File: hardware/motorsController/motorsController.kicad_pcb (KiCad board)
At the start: 2 copper layers, 12 parts, among them J1 batery_connector, M1 Motor_DC, U1 VNH5019A-E

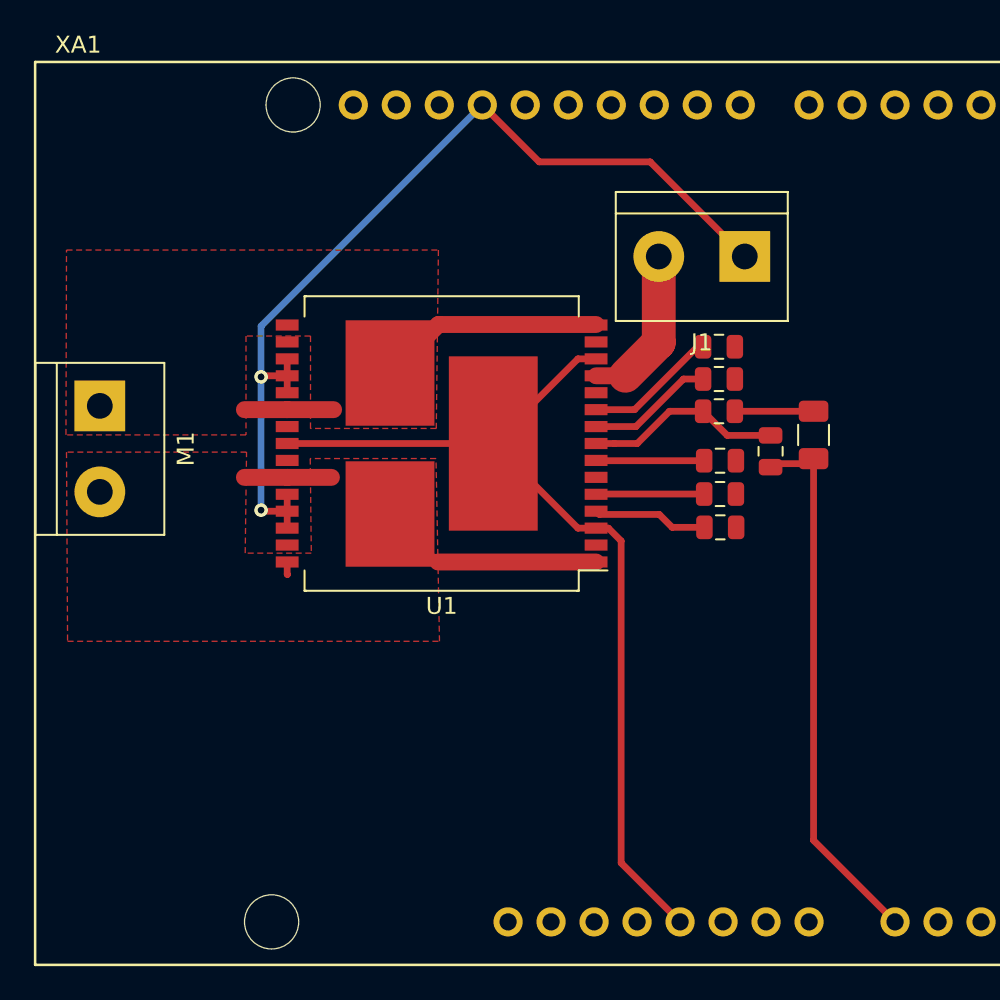
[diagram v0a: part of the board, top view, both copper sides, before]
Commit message: reposition motor terminals on both sides of the dirver
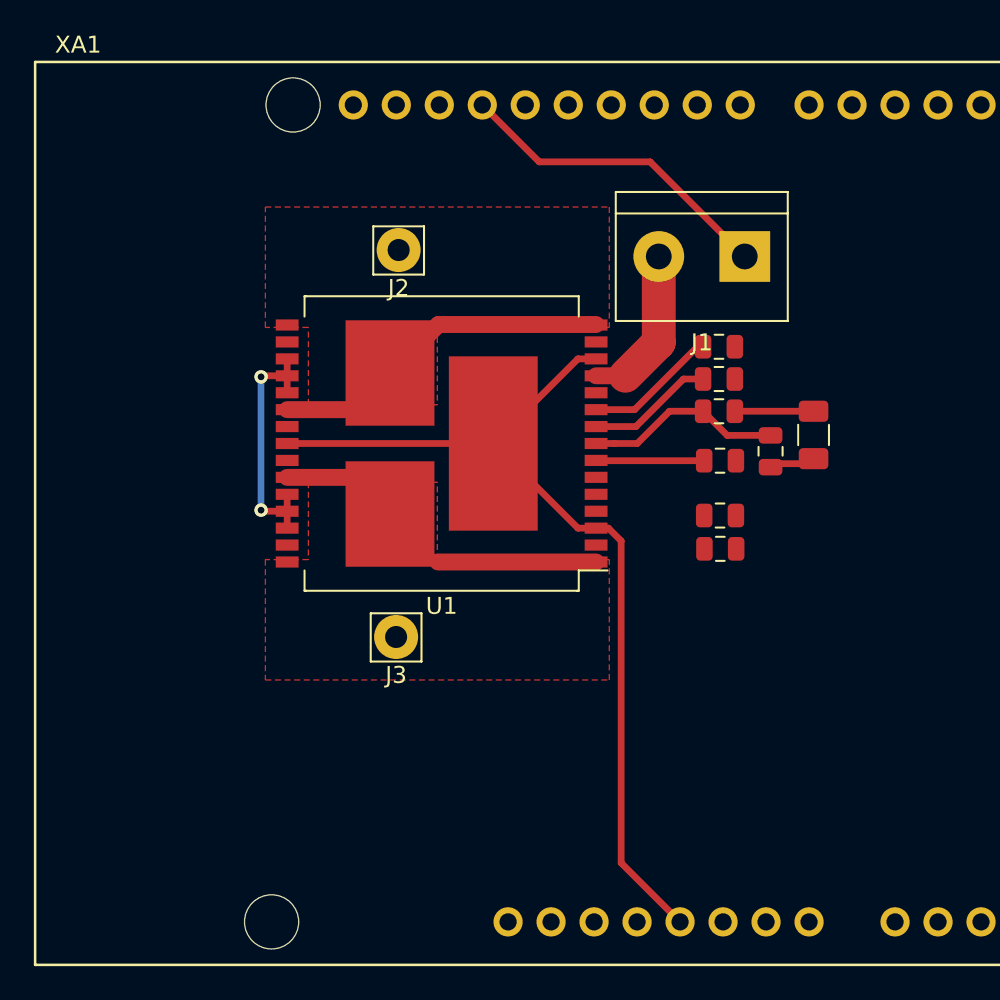
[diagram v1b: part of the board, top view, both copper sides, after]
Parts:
- removed M1: Motor_DC, TerminalBlock:TerminalBlock_bornier-2_P5.08mm
- added J2: Screw_Terminal_01x01, Connector_Pin:Pin_D1.3mm_L11.3mm_W2.8mm_Flat, F.Cu at (47.0, 38.1)
- added J3: Screw_Terminal_01x01, Connector_Pin:Pin_D1.3mm_L11.3mm_W2.8mm_Flat, F.Cu at (46.8, 61.0)
- moved R3 1.27 mm to (66.0, 55.8)
- moved R6 1.27 mm to (66.0, 53.8)
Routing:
- net /motor_right_front_cs: track 32.0 -> 2.66 mm
- net GND: track 60.4 -> 38.9 mm
- net Net-(R3-Pad1): track 6.79 -> 0.00 mm
- net Net-(R6-Pad1): track 6.39 -> 0.00 mm
- net /one_dirver/out_b: track 18.9 -> 20.3 mm
- net /one_dirver/out_a: track 19.2 -> 20.3 mm

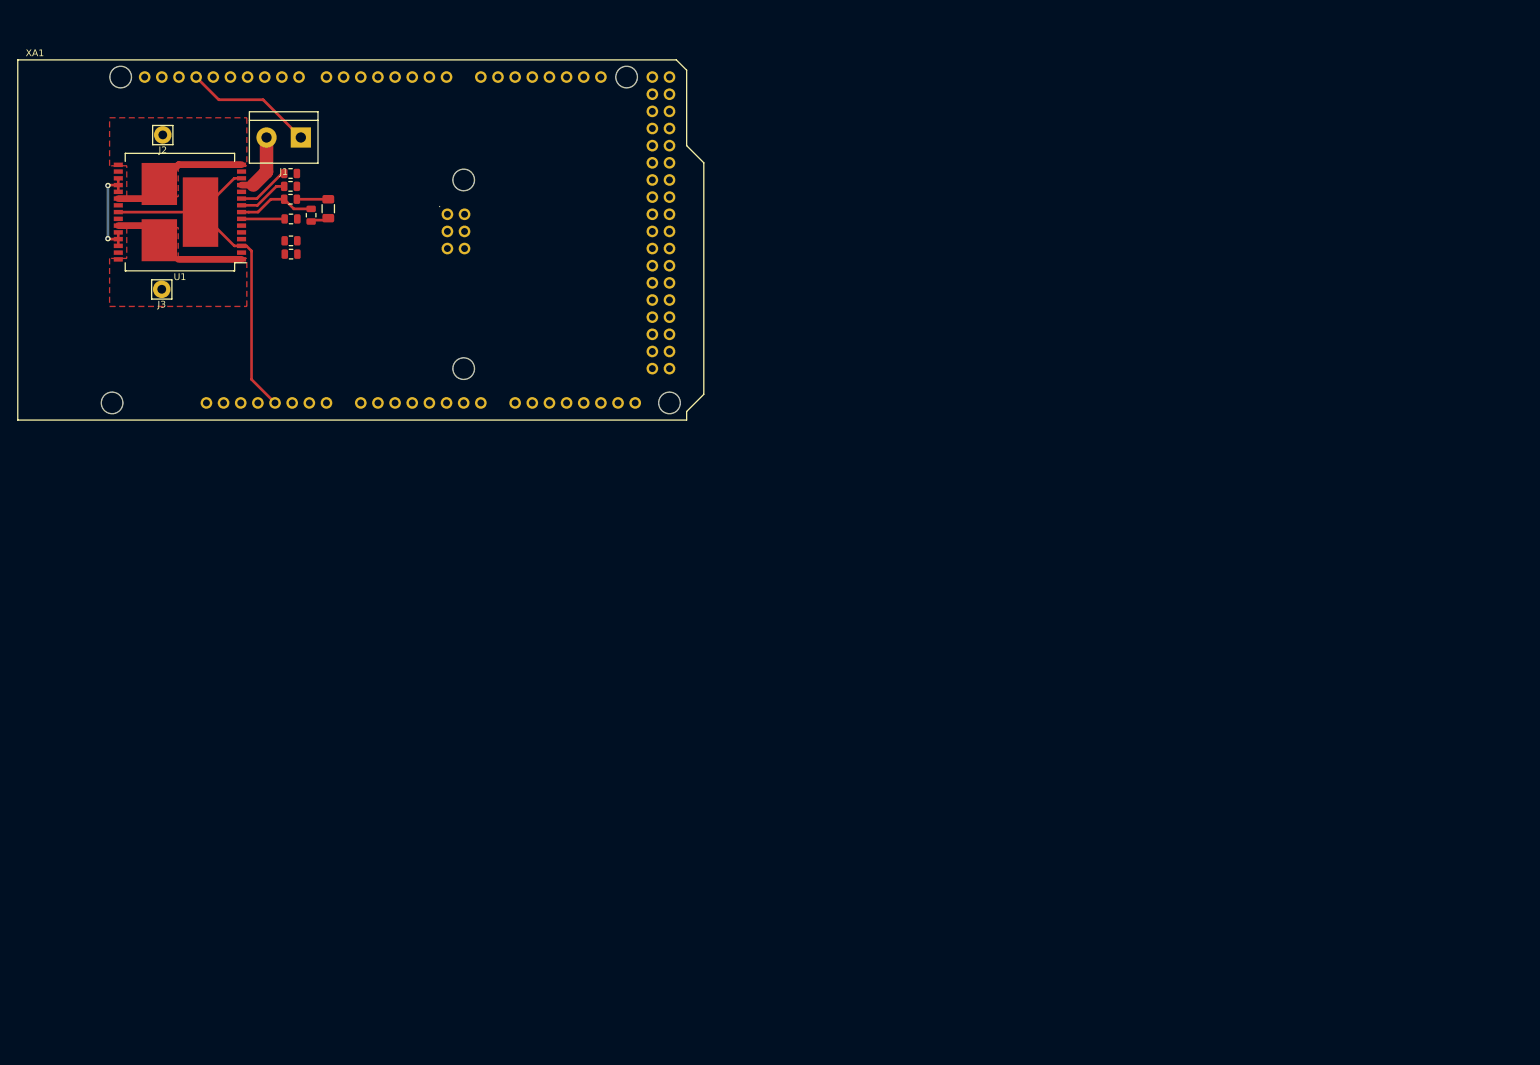
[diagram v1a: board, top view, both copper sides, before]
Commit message: re-layout power connector and components around IC
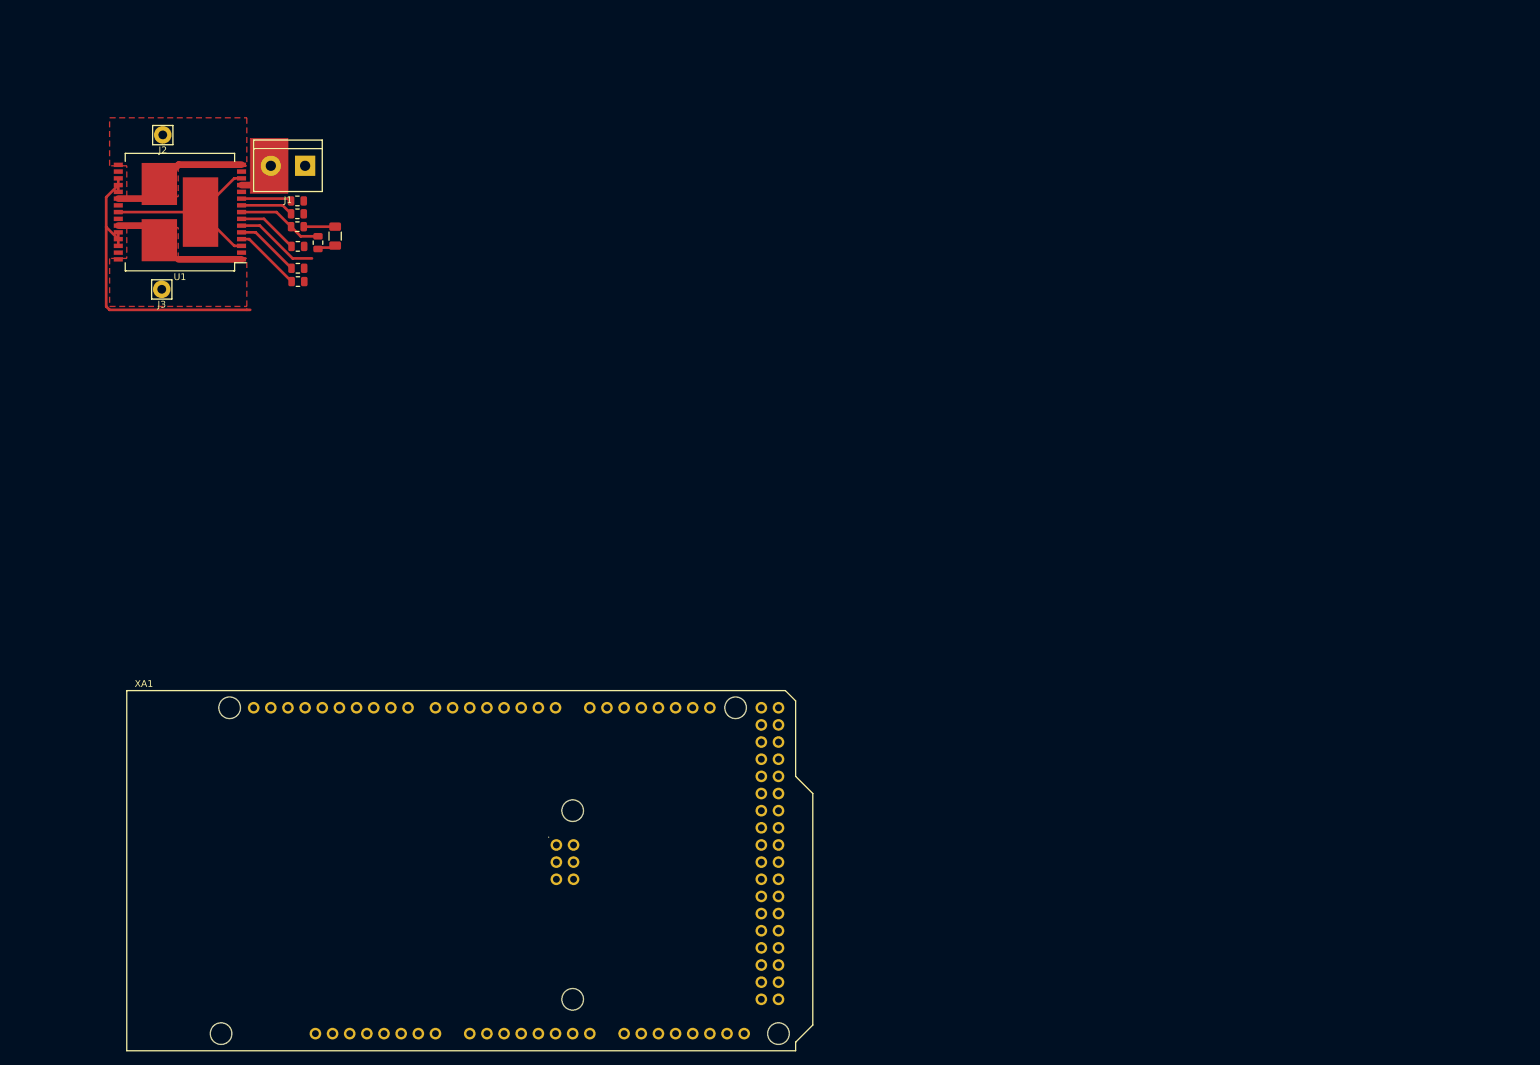
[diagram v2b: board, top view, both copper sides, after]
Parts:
- moved XA1 94.8 mm to (41.7, 173.7)
- moved J1 4.24 mm to (68.1, 42.7)
- moved R1 4.19 mm to (70.0, 54.1)
- moved R2 4.19 mm to (66.9, 51.7)
- moved R4 4.19 mm to (66.9, 47.9)
- moved R5 4.19 mm to (67.0, 54.6)
- moved R6 4.19 mm to (67.0, 57.8)
- moved R7 4.19 mm to (66.9, 49.8)
- moved C1 4.19 mm to (72.5, 53.1)
- moved R3 4.19 mm to (67.0, 59.8)
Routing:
- net +5V: track 54.2 -> 28.5 mm
- net GND: track 38.9 -> 63.9 mm, vias 2 -> 0
- net Net-(R3-Pad1): track 0.00 -> 10.0 mm
- net Net-(R6-Pad1): track 0.00 -> 9.60 mm
- net /bat+: track 9.60 -> 5.52 mm
- net Net-(R5-Pad1): track 6.39 -> 9.11 mm
- net Net-(R1-Pad1): track 12.1 -> 13.2 mm

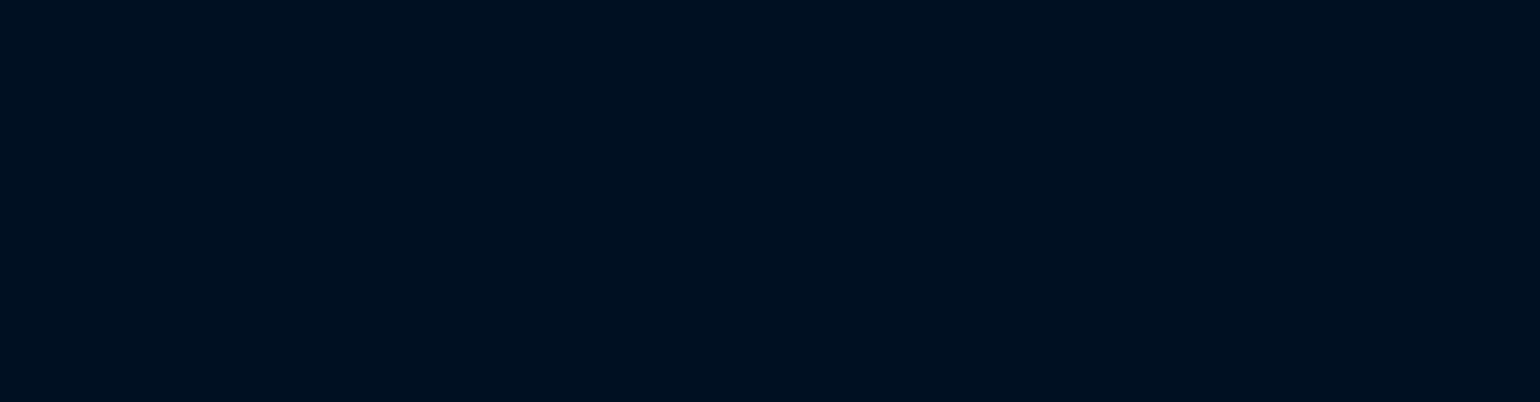
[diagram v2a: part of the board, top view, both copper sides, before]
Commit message: replicate layout for three more ICs
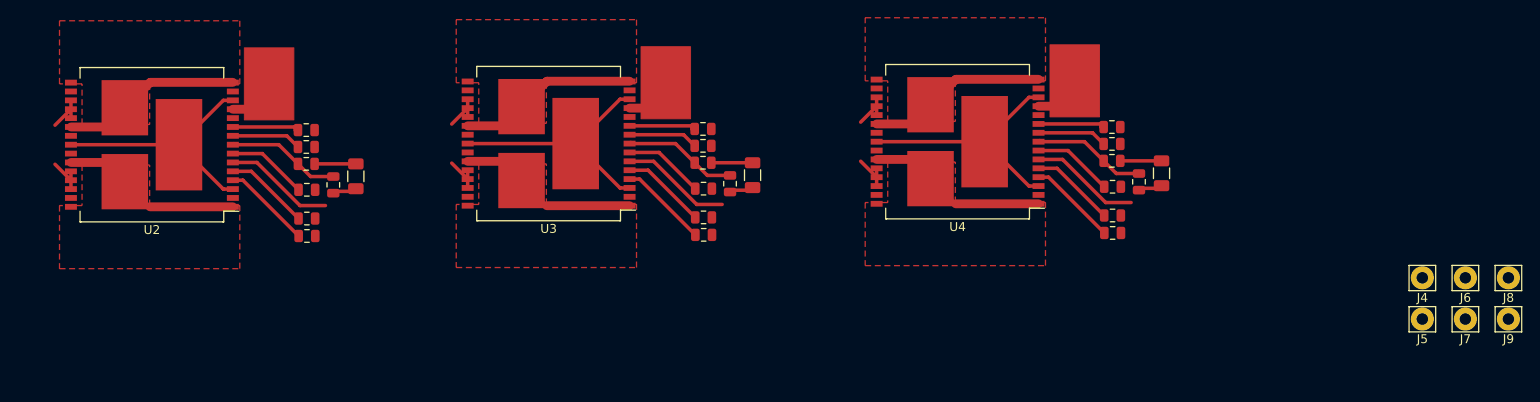
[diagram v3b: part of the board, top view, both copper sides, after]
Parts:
- added C2: 33nF, Capacitor_SMD:C_1206_3216Metric, F.Cu at (115.0, 52.9)
- added C3: 33nF, Capacitor_SMD:C_1206_3216Metric, F.Cu at (159.7, 52.8)
- added C4: 33nF, Capacitor_SMD:C_1206_3216Metric, F.Cu at (205.8, 52.6)
- added J4: Screw_Terminal_01x01, Connector_Pin:Pin_D1.3mm_L11.3mm_W2.8mm_Flat, F.Cu at (235.2, 64.3)
- added J5: Screw_Terminal_01x01, Connector_Pin:Pin_D1.3mm_L11.3mm_W2.8mm_Flat, F.Cu at (235.2, 69.0)
- added J6: Screw_Terminal_01x01, Connector_Pin:Pin_D1.3mm_L11.3mm_W2.8mm_Flat, F.Cu at (240.0, 64.3)
- added J7: Screw_Terminal_01x01, Connector_Pin:Pin_D1.3mm_L11.3mm_W2.8mm_Flat, F.Cu at (240.0, 69.0)
- added J8: Screw_Terminal_01x01, Connector_Pin:Pin_D1.3mm_L11.3mm_W2.8mm_Flat, F.Cu at (244.9, 64.3)
- added J9: Screw_Terminal_01x01, Connector_Pin:Pin_D1.3mm_L11.3mm_W2.8mm_Flat, F.Cu at (244.9, 69.0)
- added R10: 1K, Resistor_SMD:R_0805_2012Metric, F.Cu at (109.5, 59.6)
- added R11: 1K, Resistor_SMD:R_0805_2012Metric, F.Cu at (109.4, 47.7)
- added R12: 1K, Resistor_SMD:R_0805_2012Metric, F.Cu at (109.5, 54.4)
- added R13: 1K, Resistor_SMD:R_0805_2012Metric, F.Cu at (109.5, 57.7)
- added R14: 1K, Resistor_SMD:R_0805_2012Metric, F.Cu at (109.4, 49.6)
- added R15: 10K, Resistor_SMD:R_0805_2012Metric, F.Cu at (157.2, 53.7)
- added R16: 1.5K, Resistor_SMD:R_0805_2012Metric, F.Cu at (154.1, 51.4)
- added R17: 1K, Resistor_SMD:R_0805_2012Metric, F.Cu at (154.2, 59.5)
- added R18: 1K, Resistor_SMD:R_0805_2012Metric, F.Cu at (154.1, 47.6)
- added R19: 1K, Resistor_SMD:R_0805_2012Metric, F.Cu at (154.2, 54.3)
- added R20: 1K, Resistor_SMD:R_0805_2012Metric, F.Cu at (154.2, 57.5)
- added R21: 1K, Resistor_SMD:R_0805_2012Metric, F.Cu at (154.1, 49.5)
- added R22: 10K, Resistor_SMD:R_0805_2012Metric, F.Cu at (203.3, 53.5)
- added R23: 1.5K, Resistor_SMD:R_0805_2012Metric, F.Cu at (200.2, 51.2)
- added R24: 1K, Resistor_SMD:R_0805_2012Metric, F.Cu at (200.3, 59.3)
- added R25: 1K, Resistor_SMD:R_0805_2012Metric, F.Cu at (200.2, 47.3)
- added R26: 1K, Resistor_SMD:R_0805_2012Metric, F.Cu at (200.3, 54.1)
- added R27: 1K, Resistor_SMD:R_0805_2012Metric, F.Cu at (200.3, 57.3)
- added R28: 1K, Resistor_SMD:R_0805_2012Metric, F.Cu at (200.2, 49.3)
- added R8: 10K, Resistor_SMD:R_0805_2012Metric, F.Cu at (112.4, 53.9)
- added R9: 1.5K, Resistor_SMD:R_0805_2012Metric, F.Cu at (109.4, 51.5)
- added U2: VNH5019A-E, Package_SO:ST_MultiPowerSO-30, F.Cu at (92.0, 49.3)
- added U3: VNH5019A-E, Package_SO:ST_MultiPowerSO-30, F.Cu at (136.7, 49.2)
- added U4: VNH5019A-E, Package_SO:ST_MultiPowerSO-30, F.Cu at (182.8, 49.0)
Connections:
- XA1 pad A1: Net-(XA1-PadA1) -> /motor_left_front_cs
- XA1 pad A2: Net-(XA1-PadA2) -> /motor_right_rear_cs
- XA1 pad A3: Net-(XA1-PadA3) -> /motor_left_rear_cs
- XA1 pad D24: Net-(XA1-PadD24) -> /motor_left_front_back
- XA1 pad D25: Net-(XA1-PadD25) -> /motor_left_front_fwd
- XA1 pad D26: Net-(XA1-PadD26) -> /motor_right_rear_back
- XA1 pad D27: Net-(XA1-PadD27) -> /motor_right_rear_fwd
- XA1 pad D28: Net-(XA1-PadD28) -> /motor_left_rear_back
- XA1 pad D29: Net-(XA1-PadD29) -> /motor_left_rear_fwd
- XA1 pad D3: Net-(XA1-PadD3) -> /motor_left_front_pwm
- XA1 pad D32: Net-(XA1-PadD32) -> /motor_left_front_diag_a
- XA1 pad D33: Net-(XA1-PadD33) -> /motor_left_front_diag_b
- XA1 pad D34: Net-(XA1-PadD34) -> /motor_right_rear_diag_a
- XA1 pad D35: Net-(XA1-PadD35) -> /motor_right_rear_diag_b
- XA1 pad D36: Net-(XA1-PadD36) -> /motor_left_rear_diag_a
- XA1 pad D37: Net-(XA1-PadD37) -> /motor_left_rear_diag_b
- XA1 pad D4: Net-(XA1-PadD4) -> /motor_right_rear_pwm
- XA1 pad D5: Net-(XA1-PadD5) -> /motor_left_rear_pwm
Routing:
- net +5V: track 28.5 -> 113.9 mm
- net GND: track 63.9 -> 142.4 mm
- net /sheet5F8B7956/out_b: track 0.00 -> 20.3 mm
- net /sheet5F8AE5F8/out_b: track 0.00 -> 20.3 mm
- net /sheet5F8B7955/out_b: track 0.00 -> 20.3 mm
- net /sheet5F8B7956/out_a: track 0.00 -> 20.3 mm
- net /sheet5F8AE5F8/out_a: track 0.00 -> 20.3 mm
- net /sheet5F8B7955/out_a: track 0.00 -> 20.3 mm
- net /bat+: track 5.52 -> 22.1 mm
- net Net-(R15-Pad1): track 0.00 -> 13.2 mm
- net Net-(R22-Pad1): track 0.00 -> 13.2 mm
- net Net-(R8-Pad1): track 0.00 -> 13.2 mm
- net Net-(R24-Pad1): track 0.00 -> 10.0 mm
- net Net-(R17-Pad1): track 0.00 -> 10.0 mm
- net Net-(R10-Pad1): track 0.00 -> 10.0 mm
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- added copper zone on F.Cu, net /sheet5F8AE5F8/out_a
- added copper zone on F.Cu, net /sheet5F8AE5F8/out_b
- added copper zone on F.Cu, net /sheet5F8B7955/out_a
- added copper zone on F.Cu, net /sheet5F8B7955/out_b
- added copper zone on F.Cu, net /sheet5F8B7956/out_a
- added copper zone on F.Cu, net /sheet5F8B7956/out_b
